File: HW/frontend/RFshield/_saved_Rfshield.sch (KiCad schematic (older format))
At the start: 156 parts, among them P10 TXENABLE, P11 RXENABLE, P12 XTAL2, P13 GCK1, P14 GCK2, P15 SGPIO_CLK, P16 DA0, P17 DA4, P18 DA7, P19 DD0, P2 VAA, P20 DD5, P21 DD9, P22 RSSI, P23 GND, P24 GND, P25 GND, P26 GND, P27 GND, P28 GND, P29 GND, P3 SCL, P30 GND, P31 GND, P32 GND, P33 XCVR_CLKOUT, P37 INTR, P38 CLKIN, P39 CLKOUT, P4 SDA, P5 SSP1_SCK, P6 SSP1_MOSI, P7 SSP1_MISO, P8 CS_XCVR, P9 CS_AD, Q1 MOSFET_P, T1 RX_BALUN, T2 TX_BALUN, U1 MAX2837, U2 MAX5864, U3 SI5351C, X1 GSG-XTAL4PIN

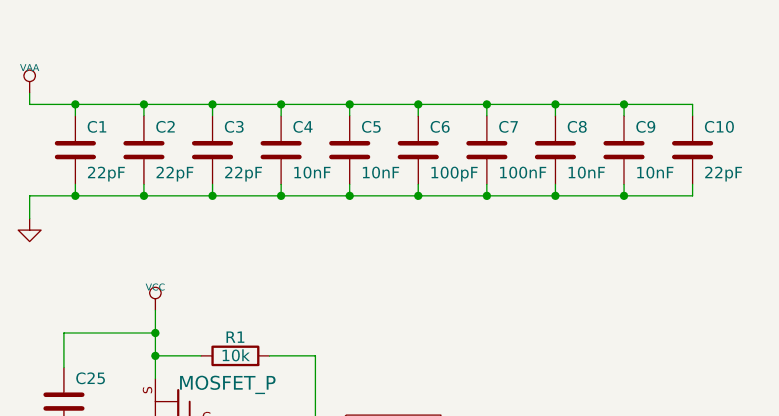
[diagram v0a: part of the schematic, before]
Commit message: components placed
components placed with reviewed footprints
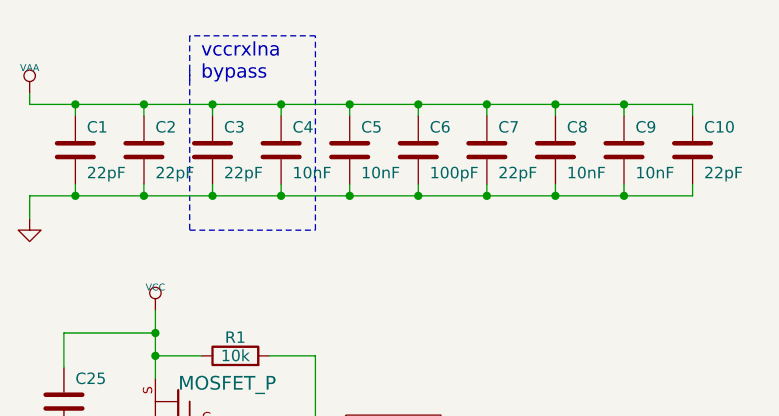
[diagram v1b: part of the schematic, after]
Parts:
- C7: value 100nF -> 22pF
- D3, D4, D5: footprint LEDs:LED-3MM -> LEDs:LED-0603
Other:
- note added: "vccrxlna \nbypass"
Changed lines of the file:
@@
 P 2700 1100
 F 0 "C7" H 2750 1200 50  0000 L CNN
-F 1 "100nF" H 2750 1000 50  0000 L CNN
+F 1 "22pF" H 2750 1000 50  0000 L CNN
 F 2 "Capacitors_SMD:C_0402" H 2700 1100 60  0001 C CNN
 F 3 "" H 2700 1100 60  0001 C CNN
@@
 F 0 "D3" H 5200 1300 50  0000 C CNN
 F 1 "LED" H 5200 1100 50  0000 C CNN
-F 2 "LEDs:LED-3MM" H 5200 1200 50  0001 C CNN
+F 2 "LEDs:LED-0603" H 5200 1200 50  0001 C CNN
 F 3 "" H 5200 1200 50  0000 C CNN
 	1    5200 1200
@@
 F 0 "D5" H 6100 1300 50  0000 C CNN
 F 1 "LED" H 6100 1100 50  0000 C CNN
-F 2 "LEDs:LED-3MM" H 6100 1200 50  0001 C CNN
+F 2 "LEDs:LED-0603" H 6100 1200 50  0001 C CNN
 F 3 "" H 6100 1200 50  0000 C CNN
 	1    6100 1200
@@
 F 0 "D4" H 5700 1300 50  0000 C CNN
 F 1 "LED" H 5700 1100 50  0000 C CNN
-F 2 "LEDs:LED-3MM" H 5700 1200 50  0001 C CNN
+F 2 "LEDs:LED-0603" H 5700 1200 50  0001 C CNN
 F 3 "" H 5700 1200 50  0000 C CNN
 	1    5700 1200
@@
 	5600 7850 5500 7850
 Connection ~ 5500 7850
+Wire Notes Line
+	1400 750  1400 1450
+Wire Notes Line
+	1400 1450 1950 1450
+Wire Notes Line
+	1950 1450 1950 600
+Wire Notes Line
+	1950 600  1400 600
+Wire Notes Line
+	1400 600  1400 800
+Text Notes 1450 800  0    60   ~ 0
+ vccrxlna \nbypass
 $EndSCHEMATC
